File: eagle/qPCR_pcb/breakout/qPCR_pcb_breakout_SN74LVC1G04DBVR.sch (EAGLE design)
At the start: 3 parts, among them U1 SN74LVC1G04DBVR

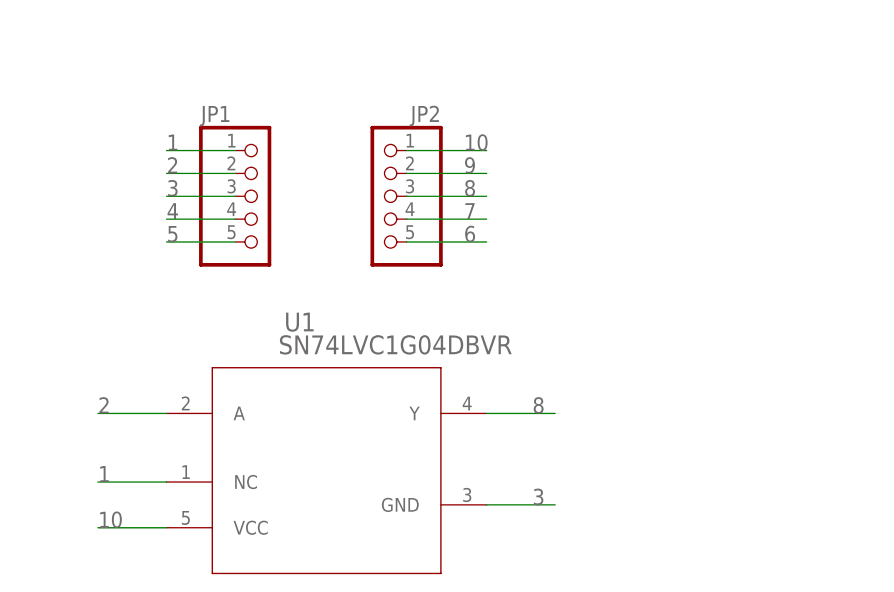
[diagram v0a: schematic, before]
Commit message: add female headers
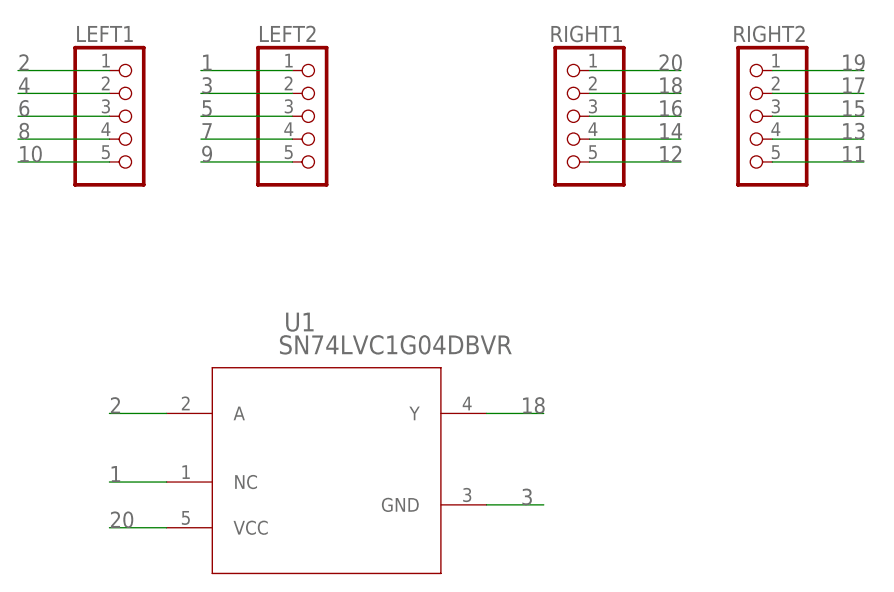
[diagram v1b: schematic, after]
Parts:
- removed JP1, JP2: (no value), pinhead:PINHD-1X5
- added LEFT1, LEFT2, RIGHT1, RIGHT2: (no value), pinhead:PINHD-1X55X2MM
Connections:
- new net 11: RIGHT2.5
- new net 12: RIGHT1.5
- new net 13: RIGHT2.4
- new net 14: RIGHT1.4
- new net 15: RIGHT2.3
- new net 16: RIGHT1.3
- new net 17: RIGHT2.2
- new net 18: RIGHT1.2, U1.Y
- new net 19: RIGHT2.1
- new net 20: RIGHT1.1, U1.VCC
- net 1: now also LEFT2.1; no longer JP1.1
- net 10: now also LEFT1.5; no longer JP2.1, U1.VCC
- net 2: now also LEFT1.1; no longer JP1.2
- net 3: now also LEFT2.2; no longer JP1.3
- net 4: now also LEFT1.2; no longer JP1.4
- net 5: now also LEFT2.3; no longer JP1.5
- net 6: now also LEFT1.3; no longer JP2.5
- net 7: now also LEFT2.4; no longer JP2.4
- net 8: now also LEFT1.4; no longer JP2.3, U1.Y
- net 9: now also LEFT2.5; no longer JP2.2

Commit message: correct footprint
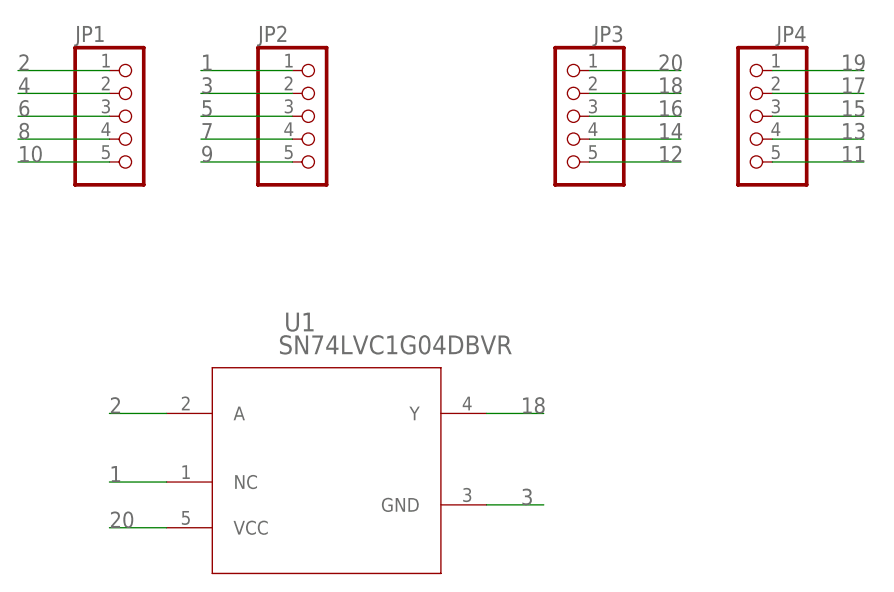
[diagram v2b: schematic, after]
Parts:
- removed LEFT1, LEFT2, RIGHT1, RIGHT2: (no value), pinhead:PINHD-1X55X2MM
- added JP1, JP2, JP3, JP4: (no value), pinhead:PINHD-1X5R
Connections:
- net 1: now also JP2.1; no longer LEFT2.1
- net 10: now also JP1.5; no longer LEFT1.5
- net 11: now also JP4.5; no longer RIGHT2.5
- net 12: now also JP3.5; no longer RIGHT1.5
- net 13: now also JP4.4; no longer RIGHT2.4
- net 14: now also JP3.4; no longer RIGHT1.4
- net 15: now also JP4.3; no longer RIGHT2.3
- net 16: now also JP3.3; no longer RIGHT1.3
- net 17: now also JP4.2; no longer RIGHT2.2
- net 18: now also JP3.2; no longer RIGHT1.2
- net 19: now also JP4.1; no longer RIGHT2.1
- net 2: now also JP1.1; no longer LEFT1.1
- net 20: now also JP3.1; no longer RIGHT1.1
- net 3: now also JP2.2; no longer LEFT2.2
- net 4: now also JP1.2; no longer LEFT1.2
- net 5: now also JP2.3; no longer LEFT2.3
- net 6: now also JP1.3; no longer LEFT1.3
- net 7: now also JP2.4; no longer LEFT2.4
- net 8: now also JP1.4; no longer LEFT1.4
- net 9: now also JP2.5; no longer LEFT2.5
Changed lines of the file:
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@@
 <parts>
 <part name="U1" library="Ninja_qPCR" library_urn="urn:adsk.eagle:library:20300418" deviceset="SN74LVC1G04DBVR" device="" package3d_urn="urn:adsk.eagle:package:20300982/2"/>
-<part name="LEFT1" library="pinhead" library_urn="urn:adsk.eagle:library:325" deviceset="PINHD-1X5" device="5X2MM" package3d_urn="urn:adsk.eagle:package:22466/2"/>
-<part name="LEFT2" library="pinhead" library_urn="urn:adsk.eagle:library:325" deviceset="PINHD-1X5" device="5X2MM" package3d_urn="urn:adsk.eagle:package:22466/2"/>
-<part name="RIGHT1" library="pinhead" library_urn="urn:adsk.eagle:library:325" deviceset="PINHD-1X5" device="5X2MM" package3d_urn="urn:adsk.eagle:package:22466/2"/>
-<part name="RIGHT2" library="pinhead" library_urn="urn:adsk.eagle:library:325" deviceset="PINHD-1X5" device="5X2MM" package3d_urn="urn:adsk.eagle:package:22466/2"/>
+<part name="JP1" library="pinhead" library_urn="urn:adsk.eagle:library:20453188" deviceset="PINHD-1X5" device="R" package3d_urn="urn:adsk.eagle:package:20453281/2"/>
+<part name="JP2" library="pinhead" library_urn="urn:adsk.eagle:library:20453188" deviceset="PINHD-1X5" device="R" package3d_urn="urn:adsk.eagle:package:20453281/2"/>
+<part name="JP3" library="pinhead" library_urn="urn:adsk.eagle:library:20453188" deviceset="PINHD-1X5" device="R" package3d_urn="urn:adsk.eagle:package:20453281/2"/>
+<part name="JP4" library="pinhead" library_urn="urn:adsk.eagle:library:20453188" deviceset="PINHD-1X5" device="R" package3d_urn="urn:adsk.eagle:package:20453281/2"/>
 </parts>
 <sheets>
@@
 <attribute name="VALUE" x="120.3706" y="44.6786" size="2.0828" layer="96" ratio="6" rot="SR0"/>
 </instance>
-<instance part="LEFT1" gate="A" x="104.14" y="71.12" smashed="yes">
+<instance part="JP1" gate="A" x="104.14" y="71.12" smashed="yes">
 <attribute name="NAME" x="97.79" y="79.375" size="1.778" layer="95"/>
 <attribute name="VALUE" x="97.79" y="60.96" size="1.778" layer="96"/>
 </instance>
-<instance part="LEFT2" gate="A" x="124.46" y="71.12" smashed="yes">
+<instance part="JP2" gate="A" x="124.46" y="71.12" smashed="yes">
 <attribute name="NAME" x="118.11" y="79.375" size="1.778" layer="95"/>
 <attribute name="VALUE" x="118.11" y="60.96" size="1.778" layer="96"/>
 </instance>
-<instance part="RIGHT1" gate="A" x="152.4" y="71.12" smashed="yes" rot="MR0">
+<instance part="JP3" gate="A" x="152.4" y="71.12" smashed="yes" rot="MR0">
 <attribute name="NAME" x="158.75" y="79.375" size="1.778" layer="95" rot="MR0"/>
 <attribute name="VALUE" x="158.75" y="60.96" size="1.778" layer="96" rot="MR0"/>
 </instance>
-<instance part="RIGHT2" gate="A" x="172.72" y="71.12" smashed="yes" rot="MR0">
+<instance part="JP4" gate="A" x="172.72" y="71.12" smashed="yes" rot="MR0">
 <attribute name="NAME" x="179.07" y="79.375" size="1.778" layer="95" rot="MR0"/>
 <attribute name="VALUE" x="179.07" y="60.96" size="1.778" layer="96" rot="MR0"/>
@@
 <net name="1" class="0">
 <segment>
-<pinref part="LEFT2" gate="A" pin="1"/>
 <wire x1="121.92" y1="76.2" x2="111.76" y2="76.2" width="0.1524" layer="91"/>
 <label x="111.76" y="76.2" size="1.778" layer="95"/>
+<pinref part="JP2" gate="A" pin="1"/>
 </segment>
 <segment>
@@
 <net name="3" class="0">
 <segment>
-<pinref part="LEFT2" gate="A" pin="2"/>
 <wire x1="121.92" y1="73.66" x2="111.76" y2="73.66" width="0.1524" layer="91"/>
 <label x="111.76" y="73.66" size="1.778" layer="95"/>
+<pinref part="JP2" gate="A" pin="2"/>
 </segment>
 <segment>
@@
 <net name="5" class="0">
 <segment>
-<pinref part="LEFT2" gate="A" pin="3"/>
 <wire x1="121.92" y1="71.12" x2="111.76" y2="71.12" width="0.1524" layer="91"/>
 <label x="111.76" y="71.12" size="1.778" layer="95"/>
+<pinref part="JP2" gate="A" pin="3"/>
 </segment>
 </net>
 <net name="7" class="0">
 <segment>
-<pinref part="LEFT2" gate="A" pin="4"/>
 <wire x1="121.92" y1="68.58" x2="111.76" y2="68.58" width="0.1524" layer="91"/>
 <label x="111.76" y="68.58" size="1.778" layer="95"/>
+<pinref part="JP2" gate="A" pin="4"/>
 </segment>
 </net>
 <net name="9" class="0">
 <segment>
-<pinref part="LEFT2" gate="A" pin="5"/>
 <wire x1="121.92" y1="66.04" x2="111.76" y2="66.04" width="0.1524" layer="91"/>
 <label x="111.76" y="66.04" size="1.778" layer="95"/>
+<pinref part="JP2" gate="A" pin="5"/>
 </segment>
 </net>
 <net name="2" class="0">
 <segment>
-<pinref part="LEFT1" gate="A" pin="1"/>
 <wire x1="101.6" y1="76.2" x2="91.44" y2="76.2" width="0.1524" layer="91"/>
 <label x="91.44" y="76.2" size="1.778" layer="95"/>
+<pinref part="JP1" gate="A" pin="1"/>
 </segment>
 <segment>
@@
 <net name="4" class="0">
 <segment>
-<pinref part="LEFT1" gate="A" pin="2"/>
 <wire x1="101.6" y1="73.66" x2="91.44" y2="73.66" width="0.1524" layer="91"/>
 <label x="91.44" y="73.66" size="1.778" layer="95"/>
+<pinref part="JP1" gate="A" pin="2"/>
 </segment>
 </net>
 <net name="6" class="0">
 <segment>
-<pinref part="LEFT1" gate="A" pin="3"/>
 <wire x1="101.6" y1="71.12" x2="91.44" y2="71.12" width="0.1524" layer="91"/>
 <label x="91.44" y="71.12" size="1.778" layer="95"/>
+<pinref part="JP1" gate="A" pin="3"/>
 </segment>
 </net>
 <net name="8" class="0">
 <segment>
-<pinref part="LEFT1" gate="A" pin="4"/>
 <wire x1="101.6" y1="68.58" x2="91.44" y2="68.58" width="0.1524" layer="91"/>
 <label x="91.44" y="68.58" size="1.778" layer="95"/>
+<pinref part="JP1" gate="A" pin="4"/>
 </segment>
 </net>
 <net name="10" class="0">
 <segment>
-<pinref part="LEFT1" gate="A" pin="5"/>
 <wire x1="101.6" y1="66.04" x2="91.44" y2="66.04" width="0.1524" layer="91"/>
 <label x="91.44" y="66.04" size="1.778" layer="95"/>
+<pinref part="JP1" gate="A" pin="5"/>
 </segment>
 </net>
 <net name="20" class="0">
 <segment>
-<pinref part="RIGHT1" gate="A" pin="1"/>
 <wire x1="154.94" y1="76.2" x2="165.1" y2="76.2" width="0.1524" layer="91"/>
 <label x="162.56" y="76.2" size="1.778" layer="95"/>
+<pinref part="JP3" gate="A" pin="1"/>
 </segment>
 <segment>
@@
 <net name="18" class="0">
 <segment>
-<pinref part="RIGHT1" gate="A" pin="2"/>
 <wire x1="154.94" y1="73.66" x2="165.1" y2="73.66" width="0.1524" layer="91"/>
 <label x="162.56" y="73.66" size="1.778" layer="95"/>
+<pinref part="JP3" gate="A" pin="2"/>
 </segment>
 <segment>
@@
 <net name="16" class="0">
 <segment>
-<pinref part="RIGHT1" gate="A" pin="3"/>
 <wire x1="154.94" y1="71.12" x2="165.1" y2="71.12" width="0.1524" layer="91"/>
 <label x="162.56" y="71.12" size="1.778" layer="95"/>
+<pinref part="JP3" gate="A" pin="3"/>
 </segment>
 </net>
 <net name="14" class="0">
 <segment>
-<pinref part="RIGHT1" gate="A" pin="4"/>
 <wire x1="154.94" y1="68.58" x2="165.1" y2="68.58" width="0.1524" layer="91"/>
 <label x="162.56" y="68.58" size="1.778" layer="95"/>
+<pinref part="JP3" gate="A" pin="4"/>
 </segment>
 </net>
 <net name="12" class="0">
 <segment>
-<pinref part="RIGHT1" gate="A" pin="5"/>
 <wire x1="154.94" y1="66.04" x2="165.1" y2="66.04" width="0.1524" layer="91"/>
 <label x="162.56" y="66.04" size="1.778" layer="95"/>
+<pinref part="JP3" gate="A" pin="5"/>
 </segment>
 </net>
 <net name="19" class="0">
 <segment>
-<pinref part="RIGHT2" gate="A" pin="1"/>
 <wire x1="175.26" y1="76.2" x2="185.42" y2="76.2" width="0.1524" layer="91"/>
 <label x="182.88" y="76.2" size="1.778" layer="95"/>
+<pinref part="JP4" gate="A" pin="1"/>
 </segment>
 </net>
 <net name="17" class="0">
 <segment>
-<pinref part="RIGHT2" gate="A" pin="2"/>
 <wire x1="175.26" y1="73.66" x2="185.42" y2="73.66" width="0.1524" layer="91"/>
 <label x="182.88" y="73.66" size="1.778" layer="95"/>
+<pinref part="JP4" gate="A" pin="2"/>
 </segment>
 </net>
 <net name="15" class="0">
 <segment>
-<pinref part="RIGHT2" gate="A" pin="3"/>
 <wire x1="175.26" y1="71.12" x2="185.42" y2="71.12" width="0.1524" layer="91"/>
 <label x="182.88" y="71.12" size="1.778" layer="95"/>
+<pinref part="JP4" gate="A" pin="3"/>
 </segment>
 </net>
 <net name="13" class="0">
 <segment>
-<pinref part="RIGHT2" gate="A" pin="4"/>
 <wire x1="175.26" y1="68.58" x2="185.42" y2="68.58" width="0.1524" layer="91"/>
 <label x="182.88" y="68.58" size="1.778" layer="95"/>
+<pinref part="JP4" gate="A" pin="4"/>
 </segment>
 </net>
 <net name="11" class="0">
 <segment>
-<pinref part="RIGHT2" gate="A" pin="5"/>
 <wire x1="175.26" y1="66.04" x2="185.42" y2="66.04" width="0.1524" layer="91"/>
 <label x="182.88" y="66.04" size="1.778" layer="95"/>
-</segment>
-</net>
+<pinref part="JP4" gate="A" pin="5"/>
+</segment>
+</net>
